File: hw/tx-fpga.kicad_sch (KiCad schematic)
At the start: 15 parts, among them U2401 ICE40UP5K-SG48ITR, Y2401 ECS-TXO-2016-33-400-TR

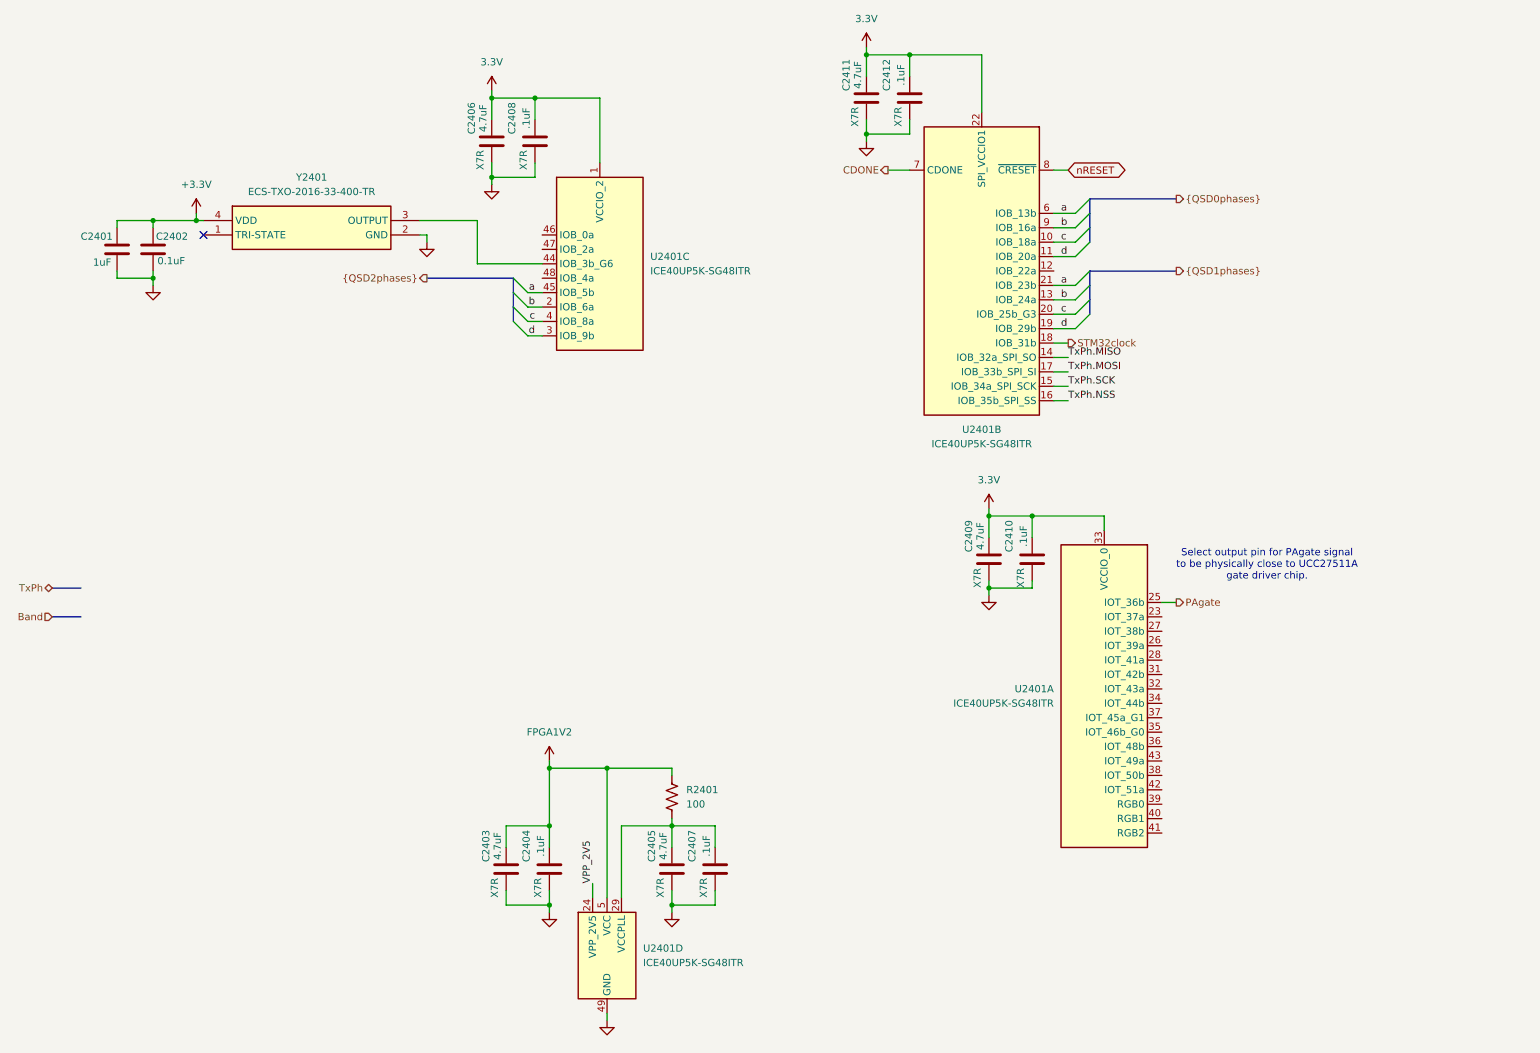
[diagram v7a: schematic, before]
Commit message: Converting to use busses as global symbols instead of tedium. Using 2n7002 Nexperia dual MOSFET because of its LOW LOW capacitance spec for L, C, and attenuator switching.
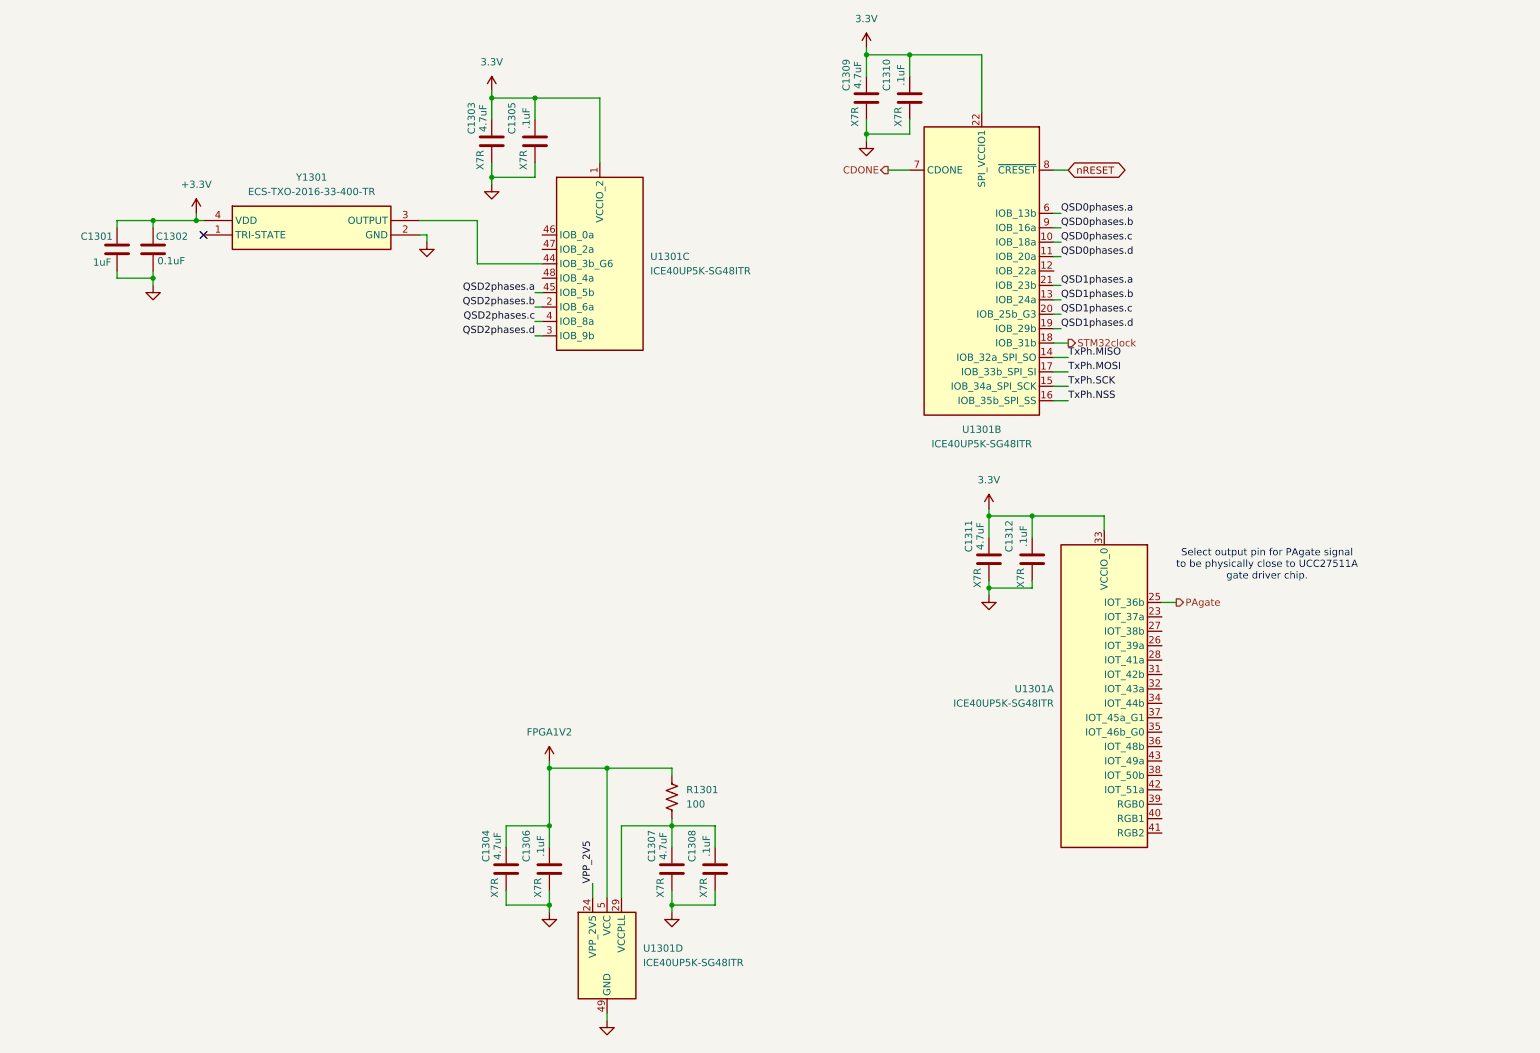
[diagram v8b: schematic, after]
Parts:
- renumbered C2401 to C1301, C2402 to C1302, C2406 to C1303, C2403 to C1304, C2408 to C1305, C2404 to C1306, C2405 to C1307, C2407 to C1308, C2411 to C1309, C2412 to C1310, C2409 to C1311, C2410 to C1312, R2401 to R1301, U2401 to U1301, Y2401 to Y1301
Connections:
- removed net a: U1301.21 (IOB_23b), U1301.45 (IOB_5b), U1301.6 (IOB_13b)
- removed net b: U1301.13 (IOB_24a), U1301.2 (IOB_6a), U1301.9 (IOB_16a)
- removed net c: U1301.10 (IOB_18a), U1301.20 (IOB_25b_G3), U1301.4 (IOB_8a)
- removed net d: U1301.11 (IOB_20a), U1301.19 (IOB_29b), U1301.3 (IOB_9b)
- new net QSD0phases.a: U1301.6 (IOB_13b)
- new net QSD0phases.b: U1301.9 (IOB_16a)
- new net QSD0phases.c: U1301.10 (IOB_18a)
- new net QSD0phases.d: U1301.11 (IOB_20a)
- new net QSD1phases.a: U1301.21 (IOB_23b)
- new net QSD1phases.b: U1301.13 (IOB_24a)
- new net QSD1phases.c: U1301.20 (IOB_25b_G3)
- new net QSD1phases.d: U1301.19 (IOB_29b)
- new net QSD2phases.a: U1301.45 (IOB_5b)
- new net QSD2phases.b: U1301.2 (IOB_6a)
- new net QSD2phases.c: U1301.4 (IOB_8a)
- new net QSD2phases.d: U1301.3 (IOB_9b)
